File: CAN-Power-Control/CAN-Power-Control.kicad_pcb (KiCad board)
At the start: 4 copper layers, 80 x 150 mm, 127 parts, among them J1 Conn_01x02_Pin, J10 Conn_02x03_Odd_Even, J11 Screw_Terminal_01x03, J12 USB_C_Receptacle, J16 Conn_02x02_Pin, J17 2601-1103, J2 8P8C, J20 2601-1102, J21 Conn_02x02_Pin, J22 2601-1103, J23 Conn_02x02_Pin, J24 2601-1103, J25 Conn_02x02_Pin, J26 2601-1103, J3 Conn_01x08_Socket, J4 2601-1102, J5 Conn_02x02_Pin, J6 2601-1102, J7 2601-1102, J8 2601-1102, J9 Screw_Terminal_01x02, K1 Power Relay AZDC007, Q1 FMMT625TA, Q2 FMMT625TA, Q3 FMMT625TA, SW1 SMD_5.2x5.2mm_h1.9mm, SW2 SMD_5.2x5.2mm_h1.9mm, U2 ACS71240LLCBTR-050U5, U3 MCP2562-E-SN, U4 LM1085-3.3, U5 TCMT4100, U6 ESP32-S3-WROOM, U7 LM1085-5.0

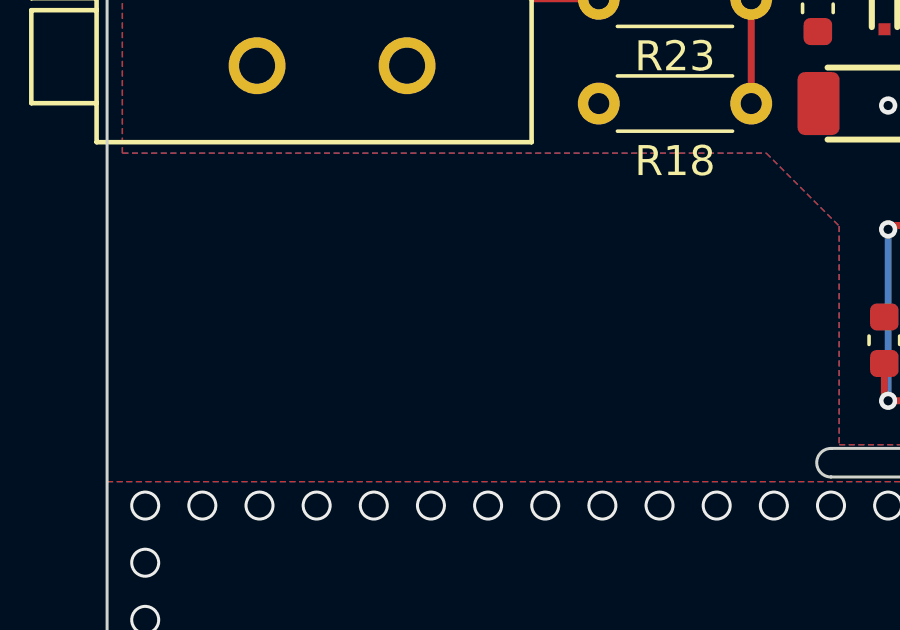
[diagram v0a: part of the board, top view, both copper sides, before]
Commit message: V01 layout almost ready for prototype
TODO:
- Ground stitching
- Double-check trace widths and 50A section
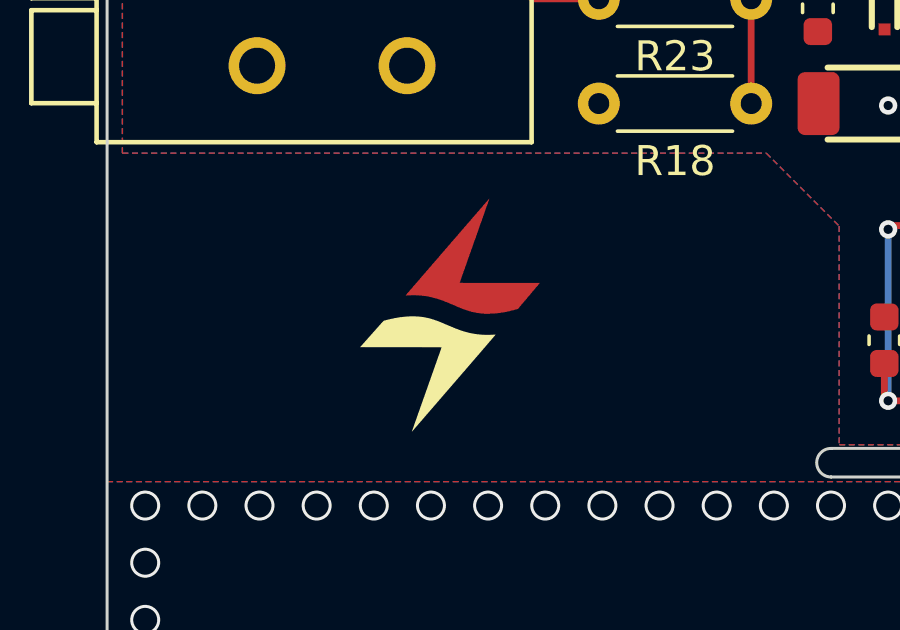
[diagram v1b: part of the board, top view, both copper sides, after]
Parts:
- added G***: LOGO, RisingTideResearch-Aesthetic:Logo_6mm_Half, F.Cu at (65.2, 141.2)

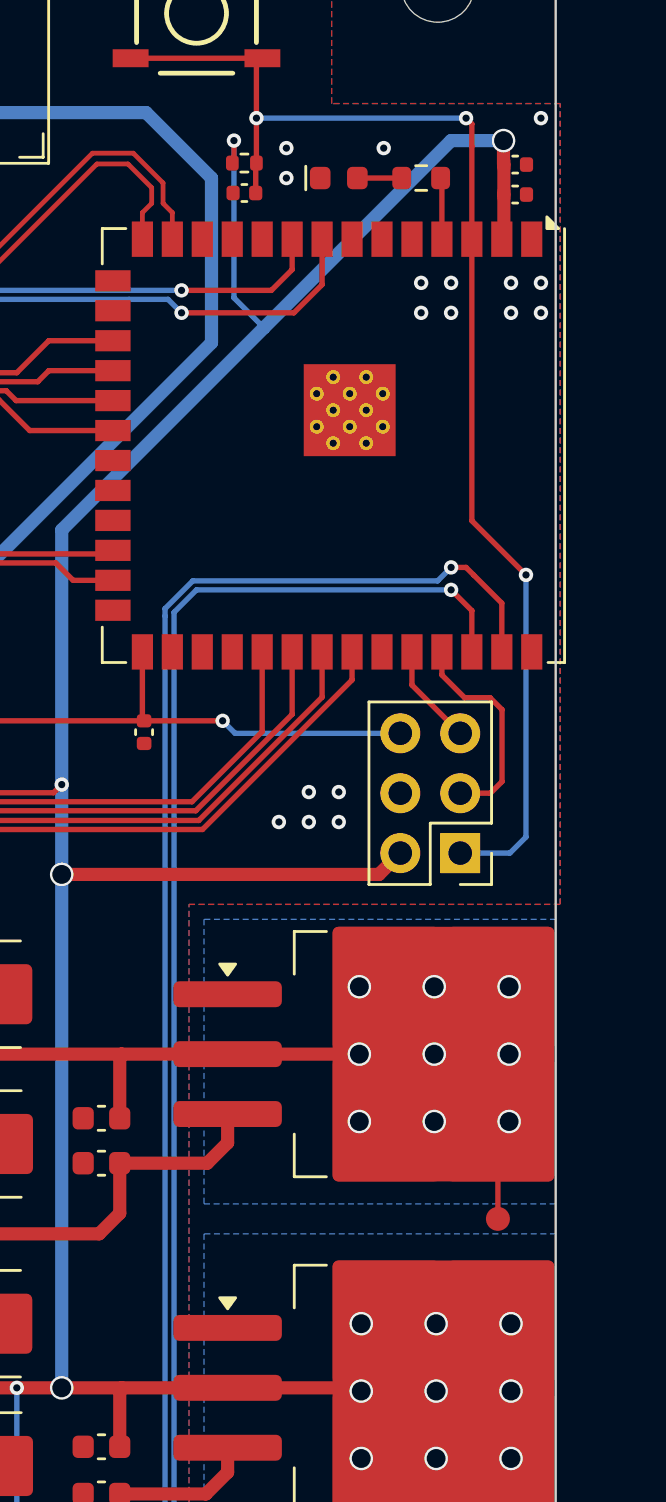
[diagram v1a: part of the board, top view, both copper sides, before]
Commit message: Minor changes
- Replace 60R resistors with closest E96 value (60.4R)
- Minor ground trace additions
- Silkscreen addition
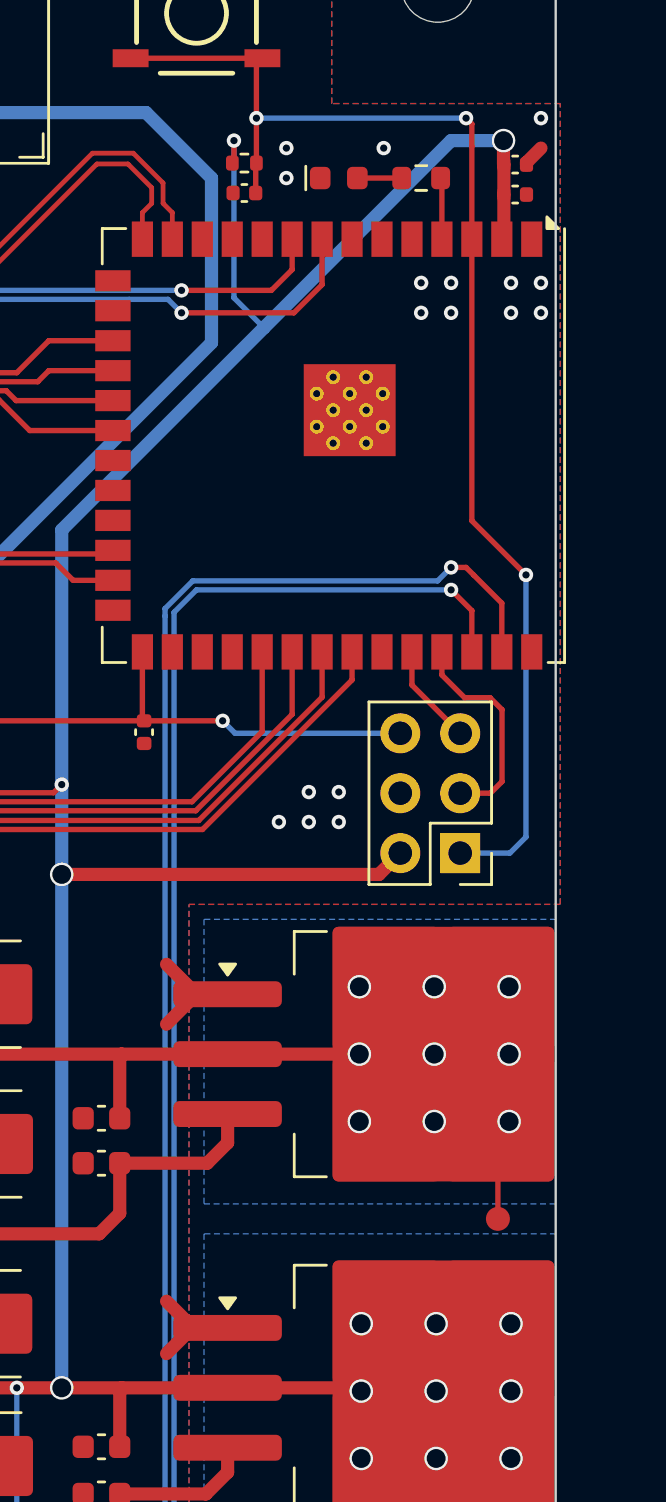
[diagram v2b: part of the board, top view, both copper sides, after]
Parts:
- added G***: LOGO, RisingTideResearch-Aesthetic:Logo_4mm, B.Cu at (119.3, 61.4)
- added kibuzzard-6881B6C9: G***, kibuzzard-6881B6C9, B.Cu at (90.8, 61.4)
- added kibuzzard-6881B704: G***, kibuzzard-6881B704, B.Cu at (94.3, 64.9)
- C20, C21: value 100uF -> 10uF
- C8: value 22uF -> 10uF
- D2: value Diode Std 650V 60A -> IDP30E65D1
- J10: value Conn_02x03_Odd_Even -> Conn 02x03 Odd Even
- J11: value Screw_Terminal_01x03 -> Screw Terminal 3Pos 12.7mm Pitch
- J12: value USB_C_Receptacle -> USB-C Receptacle
- J17, J22, J24, J26: value 2601-1103 -> WAGO 2601-1103
- J20, J4, J6, J7, J8: value 2601-1102 -> WAGO 2601-1102
- J3: value Conn_01x08_Socket -> Conn 01x08 Socket
- J9: value Screw_Terminal_01x02 -> Screw Terminal 2Pos 8.5mm Pitch
- R1: value 91R -> 1k
- R23, R25, R27, R30: value 100 -> 1k
- R36: value 1M -> 1Meg
- R39, R40: value 60 -> 60.4R
- U6: value ESP32-S3-WROOM -> ESP32-S3-WROOM-1U-N16R2
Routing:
- net GND: track 5.60 -> 17.6 mm
